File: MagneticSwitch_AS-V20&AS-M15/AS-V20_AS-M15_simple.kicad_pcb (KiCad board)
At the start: 2 copper layers, 9 x 6 mm, 5 parts

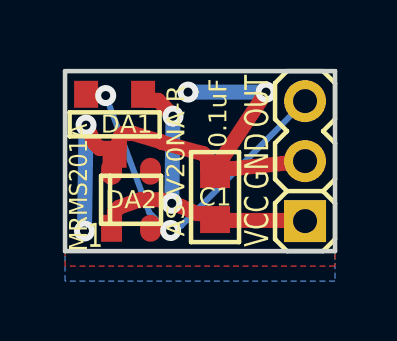
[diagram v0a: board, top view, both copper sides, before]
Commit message: AS-V20_AS-M15_simple: переход на KiCad 7
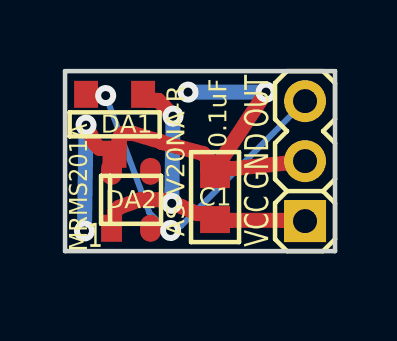
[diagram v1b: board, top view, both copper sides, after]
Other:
- net class Default removed
- net class wide removed
- net class wide wide removed
